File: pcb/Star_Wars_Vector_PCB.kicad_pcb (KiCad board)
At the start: 2 copper layers, 292.1 x 525.8 mm, 352 parts, among them J17 Main_Connector, J20 Edge_Connector_30_Pin, Q1 2N3904, Q4 2N3904, Q5 2N3904, Q6 2N3904, Q7 2N3904, Q8 2N3906

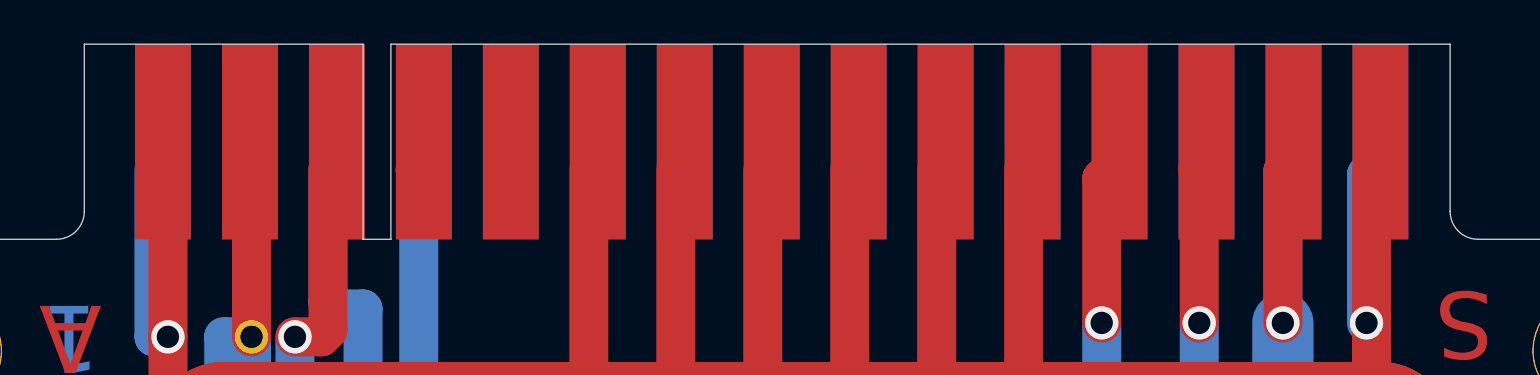
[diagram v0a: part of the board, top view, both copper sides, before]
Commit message: Fixed the solder mask on J20
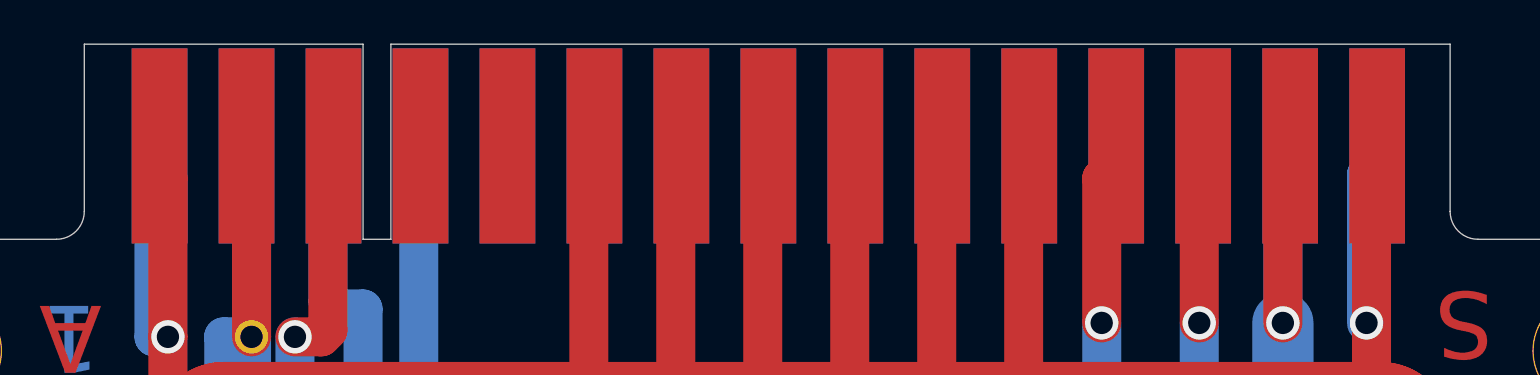
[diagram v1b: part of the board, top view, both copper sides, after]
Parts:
- moved J20 0.24 mm to (79.6, 55.4)
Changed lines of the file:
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@@
   )
   (setup
-    (last_trace_width 1.524)
+    (last_trace_width 0.25)
     (user_trace_width 0.2032)
     (user_trace_width 0.381)
@@
       (net 86 AB9))
   )
-  (module Star_Wars_Vector_PCB:J20 (layer F.Cu)
-    (at 79.7814 55.245)
-    (fp_text reference J20 (at 0.635 -10.16) (layer F.SilkS) hide
-      (effects (font (size 1 1) (thickness 0.15)))
-    )
-    (fp_text value Edge_Connector_30_Pin (at 50.165 -10.16) (layer F.Fab) hide
-      (effects (font (size 1 1) (thickness 0.15)))
-    )
-    (pad 15 smd rect (at 55.4736 -4.445) (size 2.54 8.89) (layers B.Cu F.Paste F.Mask)
-      (net 487 GND))
-    (pad 14 smd rect (at 51.5112 -4.445) (size 2.54 8.89) (layers B.Cu F.Paste F.Mask)
-      (net 4 +5V))
-    (pad 13 smd rect (at 47.5488 -4.445) (size 2.54 8.89) (layers B.Cu F.Paste F.Mask)
-      (net 469 "Net-(J20-Pad13)"))
-    (pad 12 smd rect (at 43.5864 -4.445) (size 2.54 8.89) (layers B.Cu F.Paste F.Mask)
-      (net 470 "Net-(J20-Pad12)"))
-    (pad 11 smd rect (at 39.624 -4.445) (size 2.54 8.89) (layers B.Cu F.Paste F.Mask)
-      (net 101 SPARE))
-    (pad 10 smd rect (at 35.6616 -4.445) (size 2.54 8.89) (layers B.Cu F.Paste F.Mask)
-      (net 471 X_OUT))
-    (pad 9 smd rect (at 31.6992 -4.445) (size 2.54 8.89) (layers B.Cu F.Paste F.Mask)
-      (net 472 Y_OUT))
-    (pad 8 smd rect (at 27.7368 -4.445) (size 2.54 8.89) (layers B.Cu F.Paste F.Mask)
-      (net 473 BLUE))
-    (pad 7 smd rect (at 23.7744 -4.445) (size 2.54 8.89) (layers B.Cu F.Paste F.Mask)
-      (net 474 GREEN))
-    (pad 6 smd rect (at 19.812 -4.445) (size 2.54 8.89) (layers B.Cu F.Paste F.Mask)
-      (net 475 RED))
-    (pad 5 smd rect (at 15.8496 -4.445) (size 2.54 8.89) (layers B.Cu F.Paste F.Mask)
-      (net 476 "Net-(J20-Pad5)"))
-    (pad 4 smd rect (at 11.8872 -4.445) (size 2.54 8.89) (layers B.Cu F.Paste F.Mask)
-      (net 477 -22VDC))
-    (pad 3 smd rect (at 7.9248 -4.445) (size 2.54 8.89) (layers B.Cu F.Paste F.Mask)
-      (net 478 +22VDC))
-    (pad 2 smd rect (at 3.9624 -4.445) (size 2.54 8.89) (layers B.Cu F.Paste F.Mask)
-      (net 4 +5V))
-    (pad 1 smd rect (at 0 -4.445) (size 2.54 8.89) (layers B.Cu F.Paste F.Mask)
-      (net 487 GND))
-    (pad A smd rect (at 0 -4.445) (size 2.54 8.89) (layers F.Cu F.Paste F.Mask)
-      (net 487 GND))
-    (pad B smd rect (at 3.9624 -4.445) (size 2.54 8.89) (layers F.Cu F.Paste F.Mask)
-      (net 4 +5V))
-    (pad C smd rect (at 7.9248 -4.445) (size 2.54 8.89) (layers F.Cu F.Paste F.Mask)
-      (net 103 +12V))
-    (pad D smd rect (at 11.8872 -4.445) (size 2.54 8.89) (layers F.Cu F.Paste F.Mask)
-      (net 479 "Net-(J20-PadD)"))
-    (pad E smd rect (at 15.8496 -4.445) (size 2.54 8.89) (layers F.Cu F.Paste F.Mask)
-      (net 480 "Net-(J20-PadE)"))
-    (pad F smd rect (at 19.812 -4.445) (size 2.54 8.89) (layers F.Cu F.Paste F.Mask)
-      (net 487 GND))
-    (pad H smd rect (at 23.7744 -4.445) (size 2.54 8.89) (layers F.Cu F.Paste F.Mask)
-      (net 487 GND))
-    (pad J smd rect (at 27.7368 -4.445) (size 2.54 8.89) (layers F.Cu F.Paste F.Mask)
-      (net 487 GND))
-    (pad K smd rect (at 31.6992 -4.445) (size 2.54 8.89) (layers F.Cu F.Paste F.Mask)
-      (net 487 GND))
-    (pad L smd rect (at 35.6616 -4.445) (size 2.54 8.89) (layers F.Cu F.Paste F.Mask)
-      (net 487 GND))
-    (pad M smd rect (at 39.624 -4.445) (size 2.54 8.89) (layers F.Cu F.Paste F.Mask)
-      (net 487 GND))
-    (pad N smd rect (at 43.5864 -4.445) (size 2.54 8.89) (layers F.Cu F.Paste F.Mask)
-      (net 477 -22VDC))
-    (pad P smd rect (at 47.5488 -4.445) (size 2.54 8.89) (layers F.Cu F.Paste F.Mask)
-      (net 478 +22VDC))
-    (pad R smd rect (at 51.5112 -4.445) (size 2.54 8.89) (layers F.Cu F.Paste F.Mask)
-      (net 4 +5V))
-    (pad S smd rect (at 55.4736 -4.445) (size 2.54 8.89) (layers F.Cu F.Paste F.Mask)
-      (net 487 GND))
-  )
   (module Star_Wars_Vector_PCB:TEST_POINT (layer F.Cu)
     (at 274.955 401.955 90)
@@
       (net 519 "Net-(R75-Pad1)"))
   )
+  (module Star_Wars_Vector_PCB:J20 (layer F.Cu)
+    (at 79.629 55.4355)
+    (fp_text reference J20 (at 0.635 -10.16) (layer F.SilkS) hide
+      (effects (font (size 1 1) (thickness 0.15)))
+    )
+    (fp_text value Edge_Connector_30_Pin (at 5.08 -10.16) (layer F.Fab) hide
+      (effects (font (size 1 1) (thickness 0.15)))
+    )
+    (fp_poly (pts (xy 1.27 0) (xy -1.27 0) (xy -1.27 -8.89) (xy 1.27 -8.89)) (layer B.Mask) (width 0.1))
+    (fp_poly (pts (xy 5.207 0) (xy 2.667 0) (xy 2.667 -8.89) (xy 5.207 -8.89)) (layer B.Mask) (width 0.1))
+    (fp_poly (pts (xy 9.2075 0) (xy 6.6675 0) (xy 6.6675 -8.89) (xy 9.2075 -8.89)) (layer B.Mask) (width 0.1))
+    (fp_poly (pts (xy 13.1445 0) (xy 10.6045 0) (xy 10.6045 -8.89) (xy 13.1445 -8.89)) (layer B.Mask) (width 0.1))
+    (fp_poly (pts (xy 17.0815 0) (xy 14.605 0) (xy 14.605 -8.89) (xy 17.0815 -8.89)) (layer B.Mask) (width 0.1))
+    (fp_poly (pts (xy 21.082 0) (xy 18.542 0) (xy 18.542 -8.89) (xy 21.082 -8.89)) (layer B.Mask) (width 0.1))
+    (fp_poly (pts (xy 25.019 0) (xy 22.5425 0) (xy 22.5425 -8.89) (xy 25.019 -8.89)) (layer B.Mask) (width 0.1))
+    (fp_poly (pts (xy 29.0195 0) (xy 26.4795 0) (xy 26.4795 -8.89) (xy 29.0195 -8.89)) (layer B.Mask) (width 0.1))
+    (fp_poly (pts (xy 32.9565 0) (xy 30.4165 0) (xy 30.4165 -8.89) (xy 32.9565 -8.89)) (layer B.Mask) (width 0.1))
+    (fp_poly (pts (xy 36.8935 0) (xy 34.3535 0) (xy 34.3535 -8.89) (xy 36.8935 -8.89)) (layer B.Mask) (width 0.1))
+    (fp_poly (pts (xy 40.894 0) (xy 38.354 0) (xy 38.354 -8.89) (xy 40.894 -8.89)) (layer B.Mask) (width 0.1))
+    (fp_poly (pts (xy 44.831 0) (xy 42.291 0) (xy 42.291 -8.89) (xy 44.831 -8.89)) (layer B.Mask) (width 0.1))
+    (fp_poly (pts (xy 48.768 0) (xy 46.2915 0) (xy 46.2915 -8.89) (xy 48.768 -8.89)) (layer B.Mask) (width 0.1))
+    (fp_poly (pts (xy 52.7685 0) (xy 50.2285 0) (xy 50.2285 -8.89) (xy 52.7685 -8.89)) (layer B.Mask) (width 0.1))
+    (fp_poly (pts (xy 56.7055 0) (xy 54.229 0) (xy 54.229 -8.89) (xy 56.7055 -8.89)) (layer B.Mask) (width 0.1))
+    (pad 15 smd rect (at 55.4736 -4.445) (size 2.54 8.89) (layers B.Cu F.Paste F.Mask)
+      (net 487 GND))
+    (pad 14 smd rect (at 51.5112 -4.445) (size 2.54 8.89) (layers B.Cu F.Paste F.Mask)
+      (net 4 +5V))
+    (pad 13 smd rect (at 47.5488 -4.445) (size 2.54 8.89) (layers B.Cu F.Paste F.Mask)
+      (net 469 "Net-(J20-Pad13)"))
+    (pad 12 smd rect (at 43.5864 -4.445) (size 2.54 8.89) (layers B.Cu F.Paste F.Mask)
+      (net 470 "Net-(J20-Pad12)"))
+    (pad 11 smd rect (at 39.624 -4.445) (size 2.54 8.89) (layers B.Cu F.Paste F.Mask)
+      (net 101 SPARE))
+    (pad 10 smd rect (at 35.6616 -4.445) (size 2.54 8.89) (layers B.Cu F.Paste F.Mask)
+      (net 471 X_OUT))
+    (pad 9 smd rect (at 31.6992 -4.445) (size 2.54 8.89) (layers B.Cu F.Paste F.Mask)
+      (net 472 Y_OUT))
+    (pad 8 smd rect (at 27.7368 -4.445) (size 2.54 8.89) (layers B.Cu F.Paste F.Mask)
+      (net 473 BLUE))
+    (pad 7 smd rect (at 23.7744 -4.445) (size 2.54 8.89) (layers B.Cu F.Paste F.Mask)
+      (net 474 GREEN))
+    (pad 6 smd rect (at 19.812 -4.445) (size 2.54 8.89) (layers B.Cu F.Paste F.Mask)
+      (net 475 RED))
+    (pad 5 smd rect (at 15.8496 -4.445) (size 2.54 8.89) (layers B.Cu F.Paste F.Mask)
+      (net 476 "Net-(J20-Pad5)"))
+    (pad 4 smd rect (at 11.8872 -4.445) (size 2.54 8.89) (layers B.Cu F.Paste F.Mask)
+      (net 477 -22VDC))
+    (pad 3 smd rect (at 7.9248 -4.445) (size 2.54 8.89) (layers B.Cu F.Paste F.Mask)
+      (net 478 +22VDC))
+    (pad 2 smd rect (at 3.9624 -4.445) (size 2.54 8.89) (layers B.Cu F.Paste F.Mask)
+      (net 4 +5V))
+    (pad 1 smd rect (at 0 -4.445) (size 2.54 8.89) (layers B.Cu F.Paste F.Mask)
+      (net 487 GND))
+    (pad A smd rect (at 0 -4.445) (size 2.54 8.89) (layers F.Cu F.Paste F.Mask)
+      (net 487 GND))
+    (pad B smd rect (at 3.9624 -4.445) (size 2.54 8.89) (layers F.Cu F.Paste F.Mask)
+      (net 4 +5V))
+    (pad C smd rect (at 7.9248 -4.445) (size 2.54 8.89) (layers F.Cu F.Paste F.Mask)
+      (net 103 +12V))
+    (pad D smd rect (at 11.8872 -4.445) (size 2.54 8.89) (layers F.Cu F.Paste F.Mask)
+      (net 479 "Net-(J20-PadD)"))
+    (pad E smd rect (at 15.8496 -4.445) (size 2.54 8.89) (layers F.Cu F.Paste F.Mask)
+      (net 480 "Net-(J20-PadE)"))
+    (pad F smd rect (at 19.812 -4.445) (size 2.54 8.89) (layers F.Cu F.Paste F.Mask)
+      (net 487 GND))
+    (pad H smd rect (at 23.7744 -4.445) (size 2.54 8.89) (layers F.Cu F.Paste F.Mask)
+      (net 487 GND))
+    (pad J smd rect (at 27.7368 -4.445) (size 2.54 8.89) (layers F.Cu F.Paste F.Mask)
+      (net 487 GND))
+    (pad K smd rect (at 31.6992 -4.445) (size 2.54 8.89) (layers F.Cu F.Paste F.Mask)
+      (net 487 GND))
+    (pad L smd rect (at 35.6616 -4.445) (size 2.54 8.89) (layers F.Cu F.Paste F.Mask)
+      (net 487 GND))
+    (pad M smd rect (at 39.624 -4.445) (size 2.54 8.89) (layers F.Cu F.Paste F.Mask)
+      (net 487 GND))
+    (pad N smd rect (at 43.5864 -4.445) (size 2.54 8.89) (layers F.Cu F.Paste F.Mask)
+      (net 477 -22VDC))
+    (pad P smd rect (at 47.5488 -4.445) (size 2.54 8.89) (layers F.Cu F.Paste F.Mask)
+      (net 478 +22VDC))
+    (pad R smd rect (at 51.5112 -4.445) (size 2.54 8.89) (layers F.Cu F.Paste F.Mask)
+      (net 4 +5V))
+    (pad S smd rect (at 55.4736 -4.445) (size 2.54 8.89) (layers F.Cu F.Paste F.Mask)
+      (net 487 GND))
+  )
   (gr_text K (at 226.06 88.265) (layer F.SilkS)

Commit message: Updated test points on pcb and readme file
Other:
- board text added: "Designed by Nick Mikstas"
